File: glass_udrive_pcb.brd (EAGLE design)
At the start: 8.5 x 19 mm, 14 parts, among them J1 OMNETICS_A75243-001

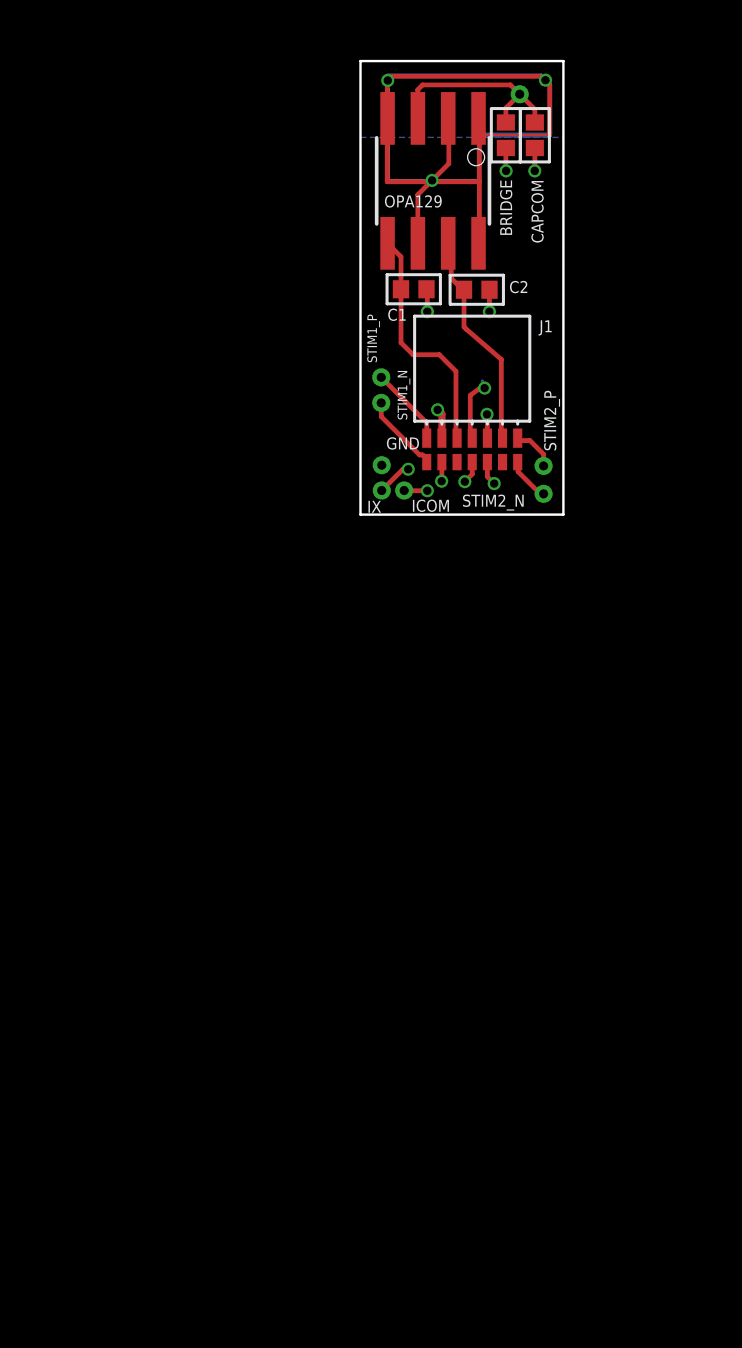
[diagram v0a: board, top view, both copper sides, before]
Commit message: Revision AD8224 redesigned to use instrumentation amplifier with a reference electrode. This version has 2 input and 2 INA output channels one for glass electrode and another for a metal electrode.
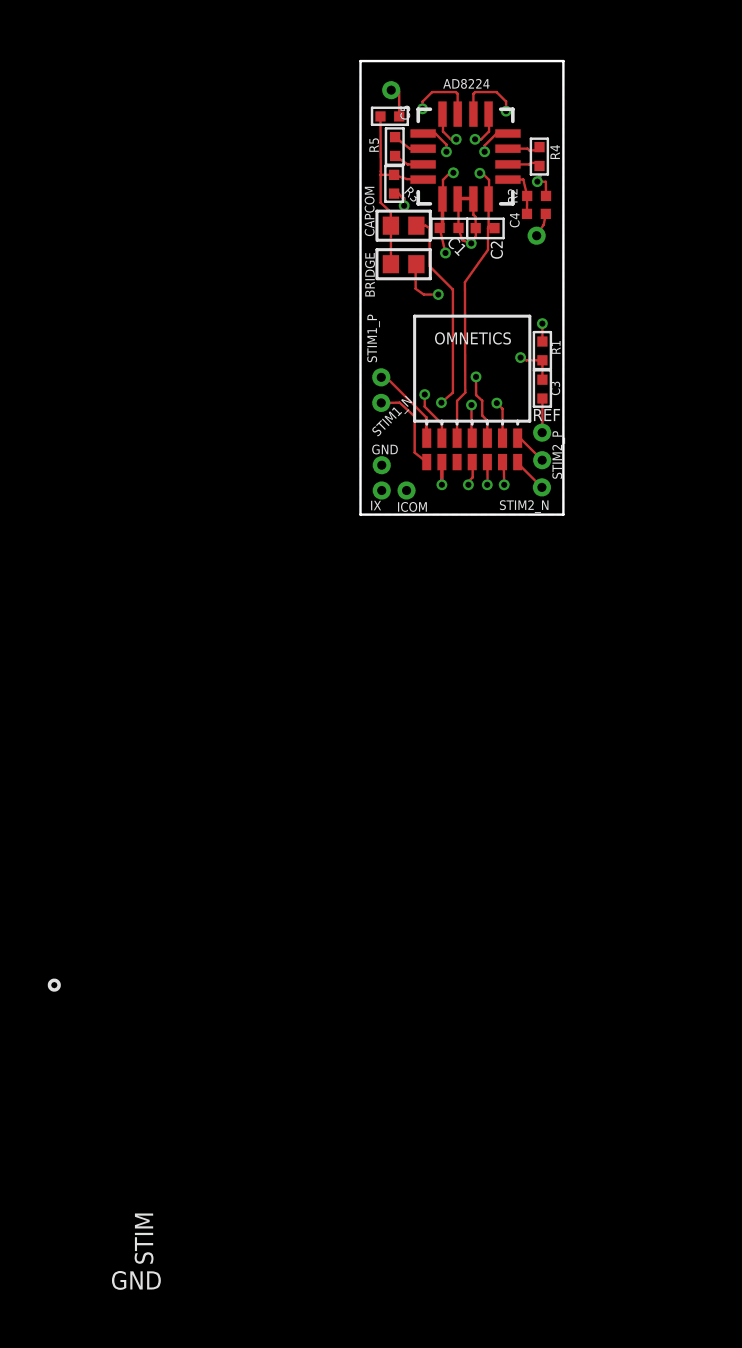
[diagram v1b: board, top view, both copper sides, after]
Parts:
- removed OPA129: OPA129U, burr-brown:SO08
- added AD8224: ANALOG-DEVICES-E14_AD8426ACPZ-R7, GyroDrive:ANALOG-DEVICES-E14_QFN65P400X400X100-16N
- added C3, C4, C5: 6800pF, GFL:0201
- added METAL, REF: (no value), GFL:30MIL/15MIL
- added R1, R3: 10Mohm, GFL:0201
- added R2: 10MOhm, GFL:0201
- added R4, R5: 5.49KOhm, GFL:0201
- C1, C2: device GFL:0402 -> GFL:0201
- moved BRIDGE 6.89 mm to (1.81, 10.5), turned to 0 degrees
- moved CAPCOM 6.68 mm to (1.81, 12.1), turned to 0 degrees
- moved GLASS 5.39 mm to (1.29, 17.8)
- moved C1 2.97 mm to (3.71, 12.0)
- moved C2 2.60 mm to (5.22, 12.0)
- moved STIM2_N 0.28 mm to (7.60, 1.14)
- moved STIM2_P 0.25 mm to (7.61, 2.28)
- moved ICOM 0.10 mm to (1.93, 1.01)
- renumbered J1 to OMNETICS
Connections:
- removed net ELECTRODE: BRIDGE.1, CAPCOM.1, GLASS.P$1, OPA129.3
- removed net SIGNAL_OUT: OMNETICS.J, OPA129.2, OPA129.6, OPA129.8
- new net GLASS: C5.1, GLASS.P$1
- new net GLASS_FLT: AD8224.4, BRIDGE.1, C5.2, CAPCOM.1, R3.2
- new net GLASS_OUT: AD8224.15, OMNETICS.J
- new net METAL: C4.1, METAL.P$1
- new net METAL_FLT: AD8224.9, C4.2, R2.2
- new net METAL_OUT: AD8224.14, OMNETICS.D
- new net N$2: AD8224.2, R5.2
- new net N$4: AD8224.3, R5.1
- new net N$6: AD8224.10, R4.2
- new net N$8: AD8224.11, R4.1
- new net REF: C3.1, REF.P$1
- new net REF_FLT: AD8224.1, AD8224.12, C3.2, R1.2
- net +15V: now also AD8224.16, AD8224.5, C1.2; no longer C2.1, OPA129.7
- net -15V: now also AD8224.13, AD8224.8, C2.2; no longer C1.2, OPA129.5
- net GND: now also AD8224.6, AD8224.7, C2.1, R1.1, R2.1, R3.1; no longer C2.2
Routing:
- net SIGNAL_OUT: track 112.0 -> 0.00 mm, vias 4 -> 0
- net GLASS_OUT: track 0.00 -> 20.5 mm, vias 0 -> 2
- net METAL_OUT: track 0.00 -> 19.7 mm, vias 0 -> 2
- net REF_FLT: track 0.00 -> 15.9 mm, vias 0 -> 3
- net ELECTRODE: track 9.29 -> 0.00 mm
- net GLASS_FLT: track 0.00 -> 8.18 mm
- net +15V: track 9.28 -> 17.0 mm, vias 0 -> 4
- net -15V: track 10.0 -> 15.7 mm, vias 0 -> 2
- net GND: track 4.72 -> 9.50 mm, vias 3 -> 5
- net BRG_BAL: track 15.4 -> 12.0 mm
- net CAP_COM: track 16.4 -> 13.0 mm
- net I_COM: track 7.66 -> 10.4 mm, vias 2 -> 1
- net METAL_FLT: track 0.00 -> 2.10 mm
- net N$8: track 0.00 -> 1.48 mm
- net N$6: track 0.00 -> 1.44 mm
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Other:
- board text added: "GND"
- board text added: "ICOM"
- board text added: "STIM"

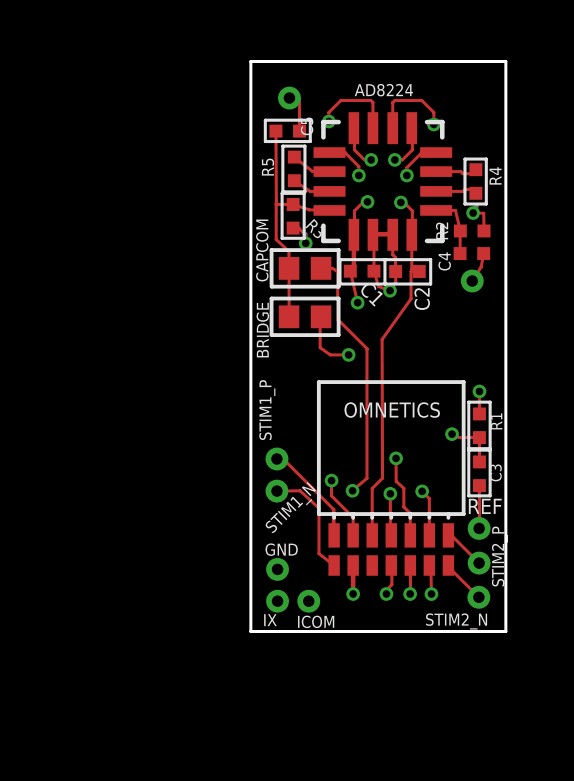
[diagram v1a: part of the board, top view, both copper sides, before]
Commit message: the modified version w/o output channel 2 and metal electrode input.
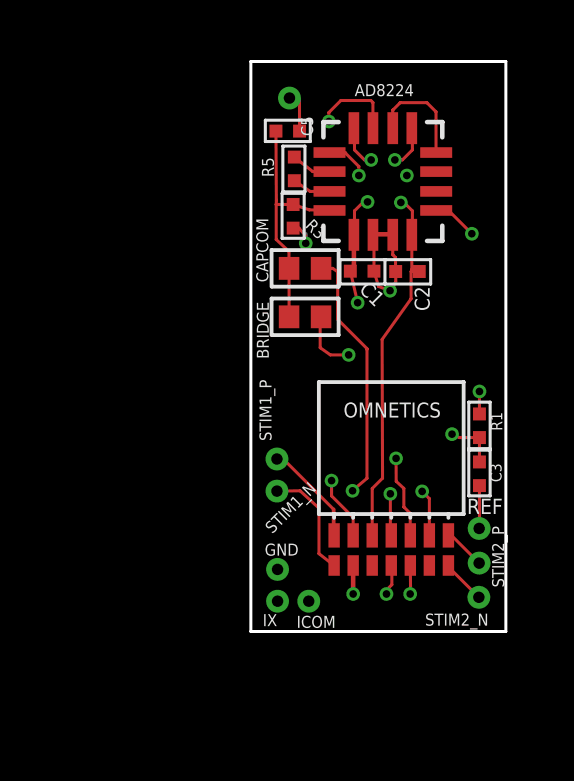
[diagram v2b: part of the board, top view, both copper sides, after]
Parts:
- removed C4: 6800pF, GFL:0201
- removed METAL: (no value), GFL:30MIL/15MIL
- removed R2: 10MOhm, GFL:0201
- removed R4: 5.49KOhm, GFL:0201
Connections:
- removed net METAL: C4.1, METAL.P$1
- removed net METAL_FLT: AD8224.9, C4.2, R2.2
- removed net N$6: AD8224.10, R4.2
- removed net N$8: AD8224.11, R4.1
- new net CHAN2_OUT: AD8224.12, AD8224.14
- net GND: now also AD8224.9; no longer R2.1
- net METAL_OUT: no longer AD8224.14
- net REF_FLT: no longer AD8224.12
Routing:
- net METAL_OUT: track 19.7 -> 0.00 mm, vias 2 -> 0
- net CHAN2_OUT: track 0.00 -> 3.62 mm
- net METAL_FLT: track 2.10 -> 0.00 mm
- net REF_FLT: track 15.9 -> 14.0 mm
- net N$8: track 1.48 -> 0.00 mm
- net N$6: track 1.44 -> 0.00 mm
- net METAL: track 1.01 -> 0.00 mm
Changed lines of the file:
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@@
 <wire x1="1.778" y1="13.1064" x2="1.0414" y2="13.1064" width="0.1016" layer="21"/>
 <wire x1="1.0414" y1="13.1064" x2="1.0414" y2="14.605" width="0.1016" layer="21"/>
-<wire x1="7.1374" y1="15.748" x2="7.8486" y2="15.748" width="0.1016" layer="21"/>
-<wire x1="7.8486" y1="15.748" x2="7.8486" y2="14.2494" width="0.1016" layer="21"/>
-<wire x1="7.8486" y1="14.2494" x2="7.1374" y2="14.2494" width="0.1016" layer="21"/>
-<wire x1="7.1374" y1="14.2494" x2="7.1374" y2="15.748" width="0.1016" layer="21"/>
 <wire x1="7.2644" y1="7.6454" x2="7.9756" y2="7.6454" width="0.1016" layer="21"/>
 <wire x1="7.9756" y1="7.6454" x2="7.9756" y2="6.096" width="0.1016" layer="21"/>
@@
 <attribute name="VALUE" x="3.355" y="14.785" size="1.27" layer="27" rot="R90"/>
 </element>
-<element name="R4" library="GFL" package="0201" value="5.49KOhm" x="7.5" y="15" smashed="yes" rot="R270">
-<attribute name="NAME" x="7.9558" y="15.505" size="0.4" layer="25" rot="R270"/>
-<attribute name="VALUE" x="5.595" y="15.635" size="1.27" layer="27" rot="R270"/>
-</element>
-<element name="METAL" library="GFL" package="30MIL/15MIL" value="" x="7.38" y="11.6838" smashed="yes">
-<attribute name="NAME" x="7.2086" y="8.9144" size="0.5" layer="26" font="vector" ratio="12" rot="MR90"/>
-<attribute name="VALUE" x="6.1608" y="10.1217" size="0.762" layer="27" font="vector" ratio="12"/>
-</element>
 <element name="R3" library="GFL" package="0201" value="10Mohm" x="1.41" y="13.84" smashed="yes" rot="R90">
 <attribute name="NAME" x="2.538" y="13.3226" size="0.4" layer="25" rot="R135"/>
 <attribute name="VALUE" x="3.315" y="13.205" size="1.27" layer="27" rot="R90"/>
 </element>
-<element name="R2" library="GFL" package="0201" value="10MOhm" x="7.378" y="13.3508" smashed="yes" rot="R180">
-<attribute name="NAME" x="6.1766" y="13.681" size="0.4" layer="25" rot="R270"/>
-<attribute name="VALUE" x="8.013" y="15.2558" size="1.27" layer="27" rot="R180"/>
-</element>
 <element name="C5" library="GFL" package="0201" value="6800pF" x="1.23" y="16.68" smashed="yes" rot="R180">
 <attribute name="NAME" x="1.675" y="17.175" size="0.4" layer="25" rot="R270"/>
 <attribute name="VALUE" x="1.865" y="18.585" size="1.27" layer="27" rot="R180"/>
-</element>
-<element name="C4" library="GFL" package="0201" value="6800pF" x="7.368" y="12.5984" smashed="yes" rot="R180">
-<attribute name="NAME" x="6.261" y="12.663" size="0.4" layer="25" rot="R270"/>
-<attribute name="VALUE" x="8.003" y="14.5034" size="1.27" layer="27" rot="R180"/>
 </element>
 <element name="R1" library="GFL" package="0201" value="10Mohm" x="7.62" y="6.858" smashed="yes" rot="R270">
@@
 <contactref element="AD8224" pad="7"/>
 <contactref element="R3" pad="1"/>
-<contactref element="R2" pad="1"/>
 <wire x1="4.68" y1="3.2034" x2="4.65" y2="3.2334" width="0.1524" layer="1"/>
 <wire x1="4.65" y1="3.2334" x2="4.65" y2="4.59" width="0.1016" layer="1"/>
@@
 <via x="1.83" y="12.94" extent="1-16" drill="0.254"/>
 <wire x1="1.83" y1="12.94" x2="1.84" y2="13.26" width="0.1016" layer="16"/>
-<via x="7.41" y="13.9492" extent="1-16" drill="0.254"/>
-<wire x1="7.41" y1="13.9492" x2="7.53" y2="14.2" width="0.1524" layer="16"/>
 <wire x1="4.7302" y1="13.222" x2="4.7122" y2="13.24" width="0.1524" layer="1"/>
 <wire x1="4.7122" y1="13.24" x2="4.09" y2="13.24" width="0.1524" layer="1"/>
@@
 <wire x1="4.1037" y1="12.01" x2="4.26" y2="11.4984" width="0.1016" layer="1"/>
 <wire x1="4.26" y1="11.4984" x2="4.64" y2="11.36" width="0.1016" layer="1"/>
-<wire x1="7.7717" y1="13.3508" x2="7.763" y2="13.9416" width="0.1016" layer="1"/>
-<wire x1="7.763" y1="13.9416" x2="7.41" y2="13.9492" width="0.1016" layer="1"/>
 <wire x1="4.0698" y1="13.222" x2="4.1037" y2="13.1881" width="0.1016" layer="1"/>
 <wire x1="4.1037" y1="13.1881" x2="4.1037" y2="12.01" width="0.1016" layer="1"/>
@@
 <wire x1="7.62" y1="8.001" x2="7.6454" y2="8.0264" width="0.1016" layer="16"/>
 <wire x1="7.6454" y1="8.0264" x2="7.5946" y2="8.0772" width="0.1016" layer="16"/>
+<contactref element="AD8224" pad="9"/>
+<wire x1="6.178" y1="14.0348" x2="6.59" y2="14.0348" width="0.1016" layer="1"/>
+<wire x1="6.59" y1="14.0348" x2="7.366" y2="13.2588" width="0.1016" layer="1"/>
+<via x="7.366" y="13.2588" extent="1-16" drill="0.254"/>
+<wire x1="7.366" y1="13.2588" x2="7.3914" y2="13.2334" width="0.1016" layer="16"/>
 </signal>
 <signal name="CAP_COM">
@@
 <wire x1="1.9752" y1="14.6698" x2="2.622" y2="14.6698" width="0.1016" layer="1"/>
 </signal>
-<signal name="N$6">
-<contactref element="AD8224" pad="10"/>
-<contactref element="R4" pad="2"/>
-<wire x1="7.5" y1="14.6063" x2="7.445" y2="14.74" width="0.1524" layer="1"/>
-<wire x1="7.445" y1="14.74" x2="7.13" y2="14.73" width="0.1016" layer="1"/>
-<wire x1="7.13" y1="14.73" x2="7.0698" y2="14.6698" width="0.1016" layer="1"/>
-<wire x1="7.0698" y1="14.6698" x2="6.178" y2="14.6698" width="0.1016" layer="1"/>
-</signal>
-<signal name="N$8">
-<contactref element="AD8224" pad="11"/>
-<contactref element="R4" pad="1"/>
-<wire x1="7.5" y1="15.3937" x2="7.495" y2="15.26" width="0.1524" layer="1"/>
-<wire x1="7.495" y1="15.26" x2="7.07" y2="15.26" width="0.1016" layer="1"/>
-<wire x1="7.07" y1="15.26" x2="6.9998" y2="15.3302" width="0.1016" layer="1"/>
-<wire x1="6.9998" y1="15.3302" x2="6.178" y2="15.3302" width="0.1016" layer="1"/>
-</signal>
 <signal name="GLASS">
 <contactref element="GLASS" pad="P$1"/>
@@
 <wire x1="1.2874" y1="17.7812" x2="1.62" y2="17.7286" width="0.1016" layer="1"/>
 <wire x1="1.62" y1="17.7286" x2="1.6237" y2="16.68" width="0.1016" layer="1"/>
-</signal>
-<signal name="METAL">
-<contactref element="METAL" pad="P$1"/>
-<contactref element="C4" pad="1"/>
-<wire x1="7.7617" y1="12.5984" x2="7.678" y2="12.1518" width="0.1016" layer="1"/>
-<wire x1="7.678" y1="12.1518" x2="7.38" y2="11.6838" width="0.1016" layer="1"/>
 </signal>
 <signal name="GLASS_OUT">
@@
 </signal>
 <signal name="METAL_OUT">
-<contactref element="AD8224" pad="14"/>
 <contactref element="OMNETICS" pad="D"/>
-<wire x1="4.7302" y1="16.778" x2="4.7302" y2="17.6302" width="0.1016" layer="1"/>
-<wire x1="4.7302" y1="17.6302" x2="4.8" y2="17.7" width="0.1016" layer="1"/>
-<wire x1="4.8" y1="17.7" x2="5.7" y2="17.7" width="0.1016" layer="1"/>
-<wire x1="5.7" y1="17.7" x2="6.1" y2="17.3" width="0.1016" layer="1"/>
-<wire x1="6.1" y1="17.3" x2="6.1" y2="16.9" width="0.1016" layer="1"/>
-<via x="6.1" y="16.9" extent="1-16" drill="0.254"/>
-<wire x1="6.1" y1="16.9" x2="6.01" y2="5.14" width="0.1016" layer="15"/>
-<wire x1="6.01" y1="5.14" x2="6.35" y2="4.83" width="0.1016" layer="15"/>
-<wire x1="6.35" y1="4.83" x2="6.35" y2="4.07" width="0.1016" layer="15"/>
-<wire x1="6.35" y1="4.07" x2="6.09" y2="3.81" width="0.1016" layer="15"/>
-<wire x1="6.09" y1="3.81" x2="6.1" y2="1.4" width="0.1016" layer="15"/>
-<wire x1="6.1" y1="1.4" x2="6.02" y2="1.2484" width="0.1016" layer="15"/>
-<via x="6.02" y="1.2484" extent="1-16" drill="0.254"/>
-<wire x1="6.02" y1="1.2484" x2="6" y2="2.1501" width="0.1016" layer="1"/>
-<wire x1="6" y1="2.1501" x2="5.95" y2="2.2001" width="0.1524" layer="1"/>
 </signal>
 <signal name="GLASS_FLT">
@@
 <wire x1="1.9502" y1="14.0548" x2="2.622" y2="14.0348" width="0.1016" layer="1"/>
 </signal>
-<signal name="METAL_FLT">
-<contactref element="AD8224" pad="9"/>
-<contactref element="R2" pad="2"/>
-<contactref element="C4" pad="2"/>
-<wire x1="6.9843" y1="13.3508" x2="6.8202" y2="14.0348" width="0.1016" layer="1"/>
-<wire x1="6.8202" y1="14.0348" x2="6.178" y2="14.0348" width="0.1016" layer="1"/>
-<wire x1="6.9743" y1="12.5984" x2="6.978" y2="13.1858" width="0.1016" layer="1"/>
-<wire x1="6.978" y1="13.1858" x2="6.9843" y2="13.3508" width="0.127" layer="1"/>
-</signal>
 <signal name="REF_FLT">
 <contactref element="AD8224" pad="1"/>
-<contactref element="AD8224" pad="12"/>
 <contactref element="C3" pad="2"/>
-<wire x1="6.178" y1="15.9652" x2="5.7352" y2="15.9652" width="0.1524" layer="1"/>
 <via x="5.2" y="15.2" extent="1-16" drill="0.254"/>
 <wire x1="5.2" y1="15.2" x2="3.6" y2="15.2" width="0.1016" layer="15"/>
 <via x="3.6" y="15.2" extent="1-16" drill="0.254"/>
 <wire x1="2.6872" y1="15.9" x2="2.622" y2="15.9652" width="0.1524" layer="1"/>
-<wire x1="5.2" y1="15.2" x2="5.2" y2="15.4616" width="0.1016" layer="1"/>
-<wire x1="5.2" y1="15.4616" x2="5.6896" y2="15.9512" width="0.1016" layer="1"/>
-<wire x1="5.6896" y1="15.9512" x2="6.164" y2="15.9512" width="0.127" layer="1"/>
-<wire x1="6.164" y1="15.9512" x2="6.178" y2="15.9652" width="0.127" layer="1"/>
 <wire x1="3.6" y1="15.2" x2="3.6" y2="15.5008" width="0.1016" layer="1"/>
 <wire x1="3.6" y1="15.5008" x2="3.1496" y2="15.9512" width="0.1016" layer="1"/>
@@
 <wire x1="5.1816" y1="15.1892" x2="5.2" y2="15.2" width="0" layer="19" extent="1-2"/>
 </signal>
+<signal name="CHAN2_OUT">
+<contactref element="AD8224" pad="14"/>
+<contactref element="AD8224" pad="12"/>
+<wire x1="4.7302" y1="16.778" x2="4.7302" y2="17.3794" width="0.1016" layer="1"/>
+<wire x1="4.7302" y1="17.3794" x2="4.9784" y2="17.6276" width="0.1016" layer="1"/>
+<wire x1="4.9784" y1="17.6276" x2="5.8674" y2="17.6276" width="0.1016" layer="1"/>
+<wire x1="5.8674" y1="17.6276" x2="6.1722" y2="17.3228" width="0.1016" layer="1"/>
+<wire x1="6.1722" y1="17.3228" x2="6.1722" y2="15.971" width="0.1016" layer="1"/>
+<wire x1="6.1722" y1="15.971" x2="6.178" y2="15.9652" width="0" layer="19" extent="1-1"/>
+</signal>
 </signals>
